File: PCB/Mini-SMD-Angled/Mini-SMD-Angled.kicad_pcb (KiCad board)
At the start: 2 copper layers, 65.1 x 96.9 mm, 35 parts, among them J1 Daisy port out, J2 ICSP_ISP6, J3 2-pin header, J4 Daisy port in, J5 Ext. MicroSD module, J6 2-pin header, K1 HYC77-TF09-200, U1 PC817C-S, U2 ATmega328P-AU, U3 SE5218, U4 TXB0104PWR, Y1 Resonator_GND2

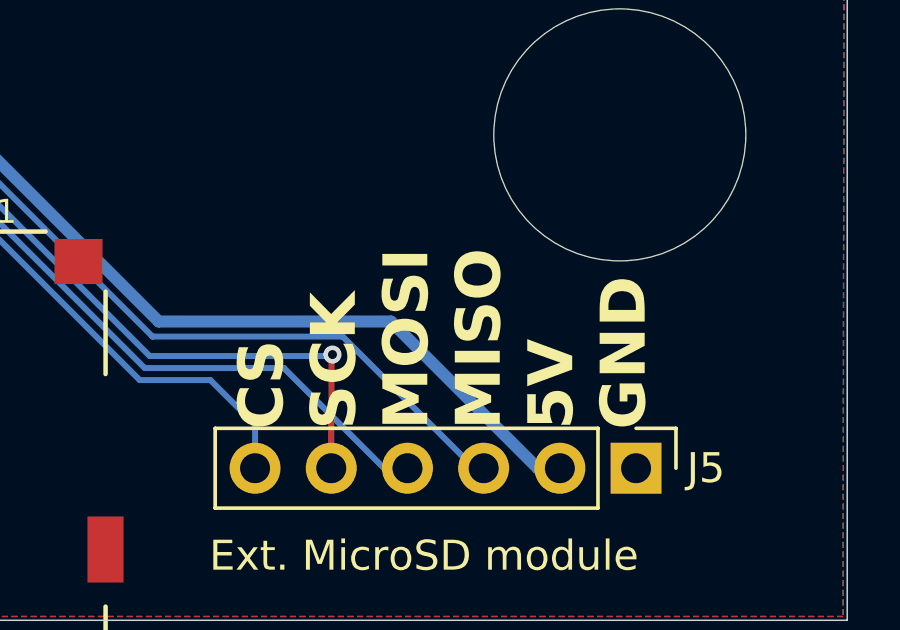
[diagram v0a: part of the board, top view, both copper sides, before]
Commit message: Make PCBs closer to one another
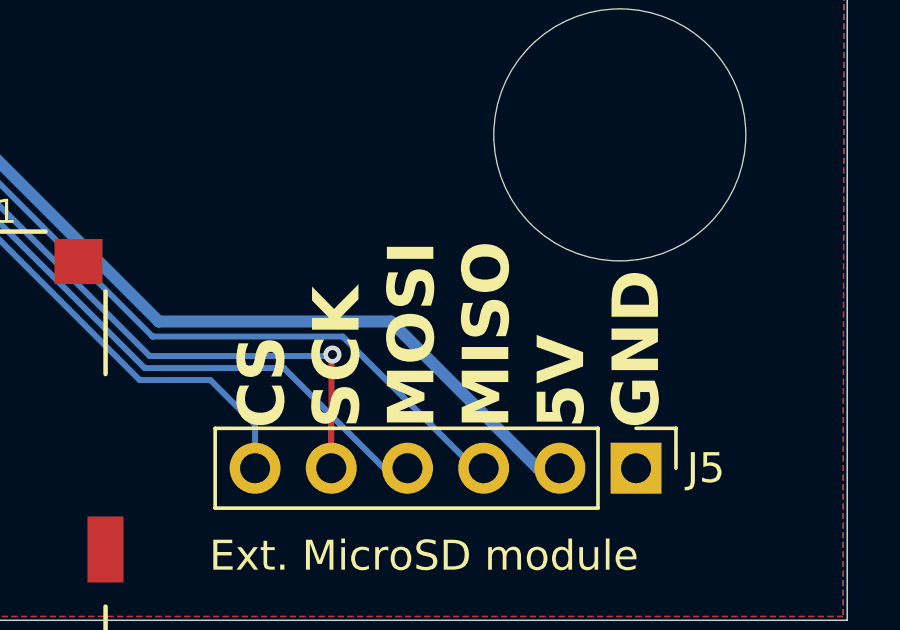
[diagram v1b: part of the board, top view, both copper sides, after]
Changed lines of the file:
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@@
 	)
 	(gr_text "CS\nSCK\nMOSI\nMISO\n5V\nGND"
-		(at 158.06 133.9 90)
+		(at 158.51 133.86 90)
 		(layer "F.SilkS")
 		(effects
 			(font
-				(size 1.5 1.5)
-				(thickness 0.3)
+				(size 1.55 1.55)
+				(thickness 0.31)
 				(bold yes)
 			)

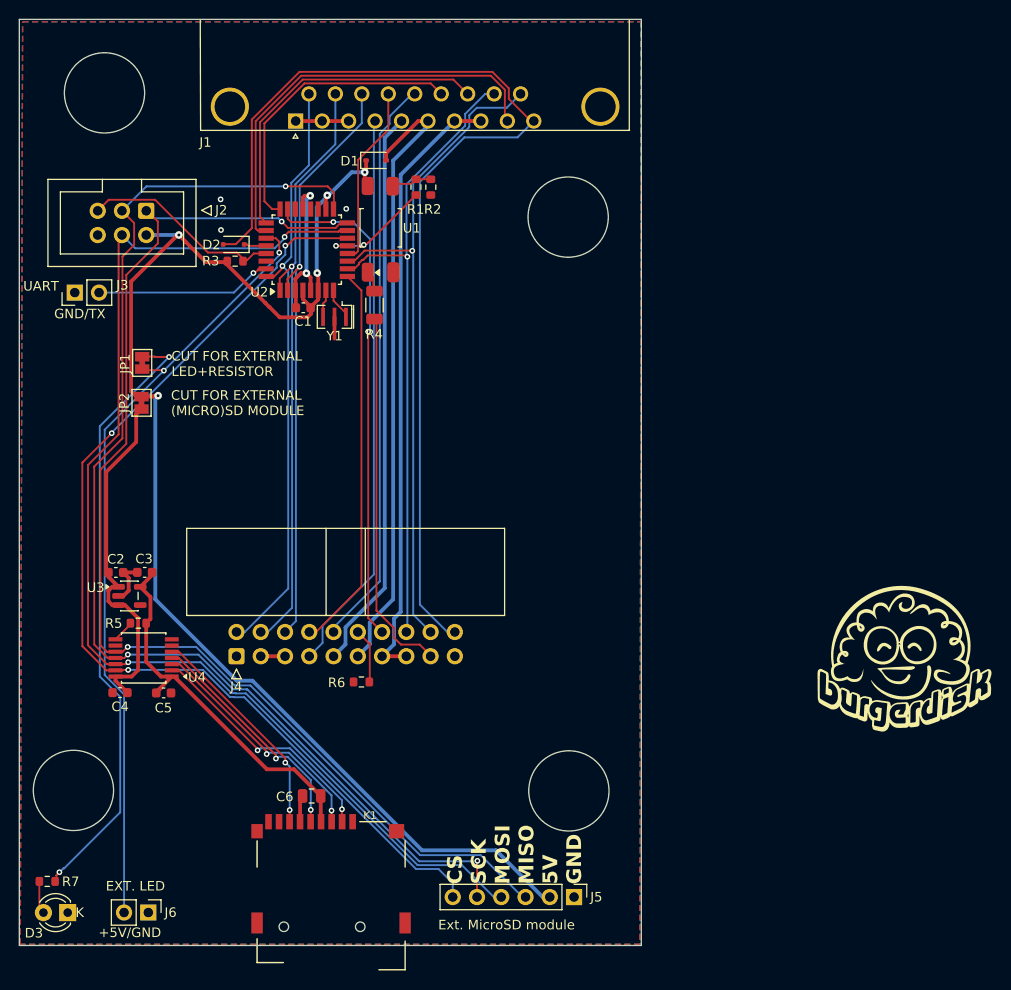
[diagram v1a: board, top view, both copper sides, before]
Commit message: Put the logo back on the PCB
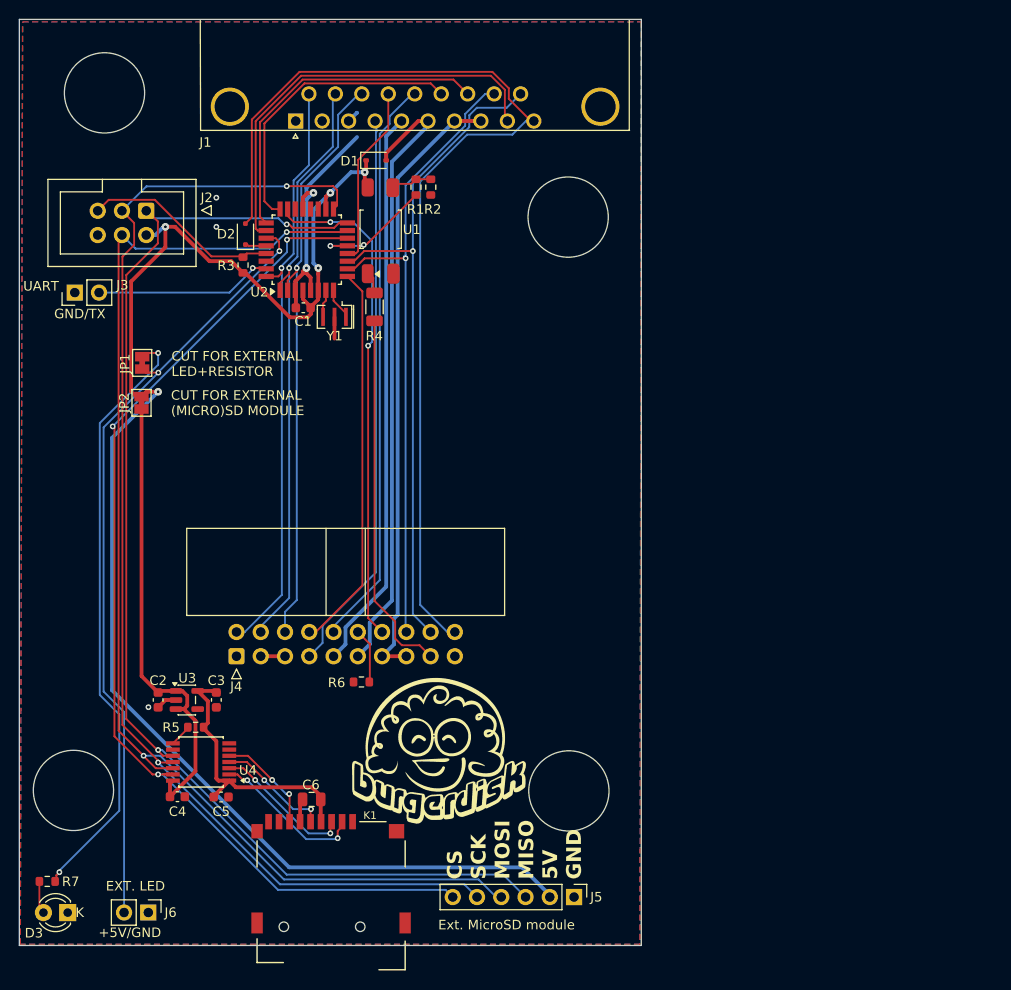
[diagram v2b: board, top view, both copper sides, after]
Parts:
- moved G*** 49.7 mm to (143.4, 119.9)
- moved C3 15.3 mm to (120.1, 114.6), turned to 90 degrees
- moved C2 14.1 mm to (114.0, 114.6), turned to 90 degrees
- moved C5 12.4 mm to (120.6, 124.7)
- moved R5 12.4 mm to (118.0, 117.4)
- moved U4 12.4 mm to (118.5, 121.1)
- moved U3 12.4 mm to (117.1, 114.6)
- moved C4 12.4 mm to (116.1, 124.7), turned to 180 degrees
- moved D2 1.64 mm to (123.2, 65.8), turned to 90 degrees
- moved R3 0.92 mm to (122.9, 69.0), turned to 90 degrees
- moved C6 0.36 mm to (130.1, 125.0)
- moved R4 0.19 mm to (136.7, 73.4)
- moved U1 0.15 mm to (137.3, 65.3)
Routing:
- net 5V_burgerDisk: track 142.1 -> 156.0 mm
- net SCLK_L: track 24.5 -> 12.0 mm
- net MISO_L: track 23.3 -> 10.8 mm
- net 5V_intMicroSD: track 36.8 -> 48.7 mm
- net MOSI_L: track 25.5 -> 14.7 mm
- net 3V3: track 40.0 -> 29.9 mm
- net CS_L: track 25.9 -> 16.2 mm
- net MOSI: track 123.4 -> 127.4 mm
- net WRPROT_out: track 112.8 -> 108.9 mm
- net GND: track 34.3 -> 37.2 mm
- net MISO: track 125.9 -> 128.3 mm
- net CS: track 108.1 -> 110.5 mm
- net Net-(JP1-A): track 64.3 -> 63.1 mm
- net DRV2_burgerDisk: track 11.8 -> 12.9 mm
- net PH0: track 62.8 -> 62.3 mm
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
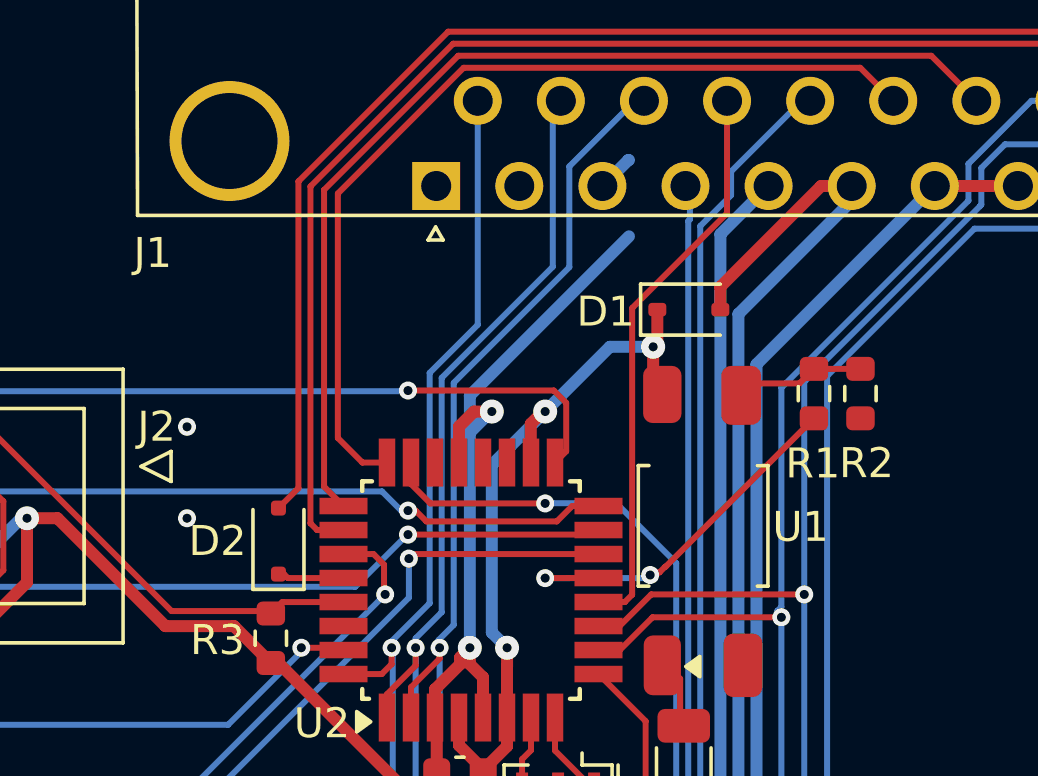
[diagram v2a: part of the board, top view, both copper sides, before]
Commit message: Move to bigger pads for diodes
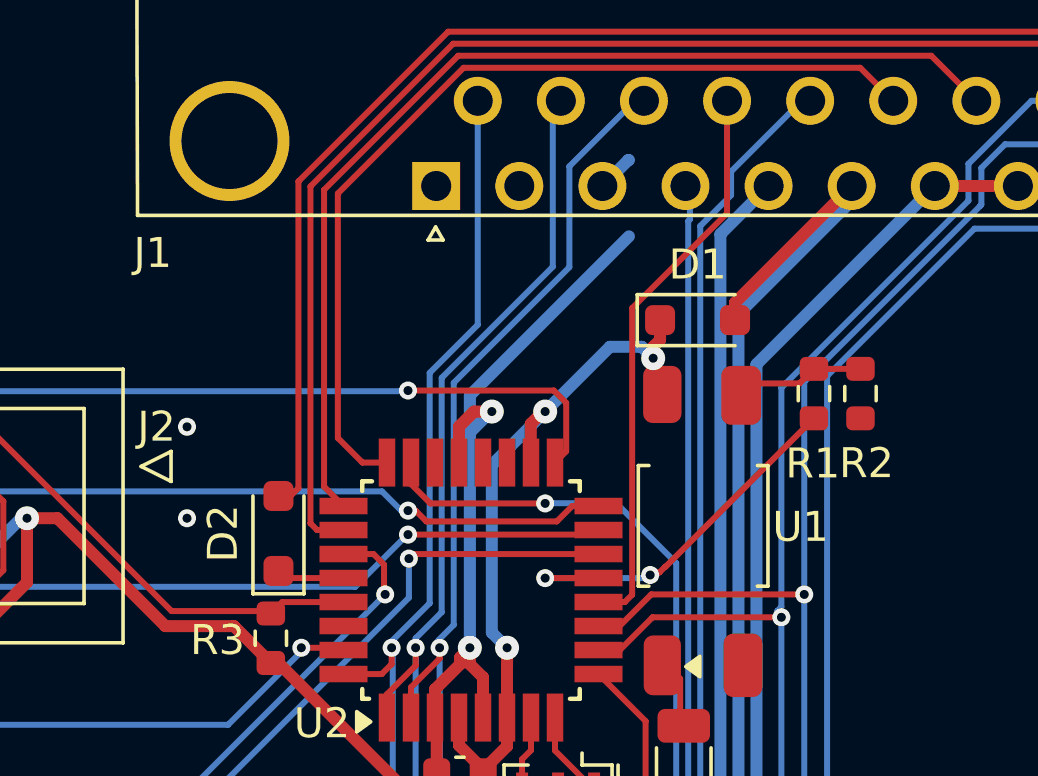
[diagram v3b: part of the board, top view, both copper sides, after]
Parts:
- D1: footprint Diode_SMD:D_SOD-323 -> Diode_SMD:D_SOD-323_HandSoldering
- D2: footprint Diode_SMD:D_SOD-323F -> Diode_SMD:D_SOD-323_HandSoldering
- moved D1 0.45 mm to (137.2, 58.4)
- moved D2 0.25 mm to (123.2, 65.5)
